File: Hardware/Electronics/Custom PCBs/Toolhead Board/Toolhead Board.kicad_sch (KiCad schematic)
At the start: 6 parts, among them U1 SE8650X2-HF, U2 XC6206P332MR

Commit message: Make some updates
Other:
- added sheet Load Cell Amplifiers (amps.kicad_sch)
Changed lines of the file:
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@@
     )
   )
-  (sheet (at 115.57 58.42) (size 12.7 3.81) (fields_autoplaced)
+  (sheet (at 95.25 19.05) (size 12.7 3.81) (fields_autoplaced)
     (stroke (width 0.1524) (type solid))
     (fill (color 0 0 0 0.0000))
-    (property "Sheetname" "Stepper Driver" (at 115.57 57.7084 0)
+    (property "Sheetname" "Stepper Driver" (at 95.25 18.3384 0)
       (effects (font (size 1.27 1.27)) (justify left bottom))
     )
-    (property "Sheetfile" "stepper.kicad_sch" (at 115.57 62.8146 0)
+    (property "Sheetfile" "stepper.kicad_sch" (at 95.25 23.4446 0)
       (effects (font (size 1.27 1.27)) (justify left top))
     )
@@
       )
     )
+  )
+  (sheet (at 100.33 35.56) (size 12.7 3.81) (fields_autoplaced)
+    (stroke (width 0.1524) (type solid))
+    (fill (color 0 0 0 0.0000))
+    (property "Sheetname" "Load Cell Amplifiers" (at 100.33 34.8484 0)
+      (effects (font (size 1.27 1.27)) (justify left bottom))
+    )
+    (property "Sheetfile" "amps.kicad_sch" (at 100.33 39.9546 0)
+      (effects (font (size 1.27 1.27)) (justify left top))
+    )
+    (instances
+      (project "Toolhead Board"
+        (path "/a1747683-152e-4245-ab61-2d33ce6021ef" (page "5"))
+      )
+    )

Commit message: some updates
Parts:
- C1: renamed from C10; footprint Capacitor_SMD:C_0805_2012Metric -> (none); Digikey (none) -> 4713-GMC21X7R105K50NTCT-ND
- C2: renamed from C11; footprint Capacitor_SMD:C_0402_1005Metric -> (none)
- C3: renamed from C12; footprint Capacitor_SMD:C_0402_1005Metric -> (none)
- C4: renamed from C13; footprint Capacitor_SMD:C_0402_1005Metric -> (none)
- U1: value SE8650X2-HF -> LF15_TO220; footprint Package_TO_SOT_SMD:SOT-23 -> Package_TO_SOT_THT:TO-220-3_Vertical
- U2: value XC6206P332MR -> LF15_TO220; footprint Package_TO_SOT_SMD:SOT-23 -> Package_TO_SOT_THT:TO-220-3_Vertical
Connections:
- net +24V: now also U1.1 (VI); no longer U1.3 (VI)
- net +3.3V: now also U2.3 (VO); no longer U2.2 (VO)
- net +5V: now also U1.3 (VO), U2.1 (VI); no longer U1.2 (VO), U2.3 (VI)
- net GND: now also U1.2 (GND), U2.2 (GND); no longer U1.1 (GND), U2.1 (GND)
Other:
- moved on the sheet: C1, C2, C3, C4, U1, U2

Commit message: Work on toolhead board more
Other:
- added sheet Accelerometer (accel.kicad_sch)
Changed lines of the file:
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@@
+    )
+  )
+  (sheet (at 48.26 31.75) (size 12.7 3.81) (fields_autoplaced)
+    (stroke (width 0.1524) (type solid))
+    (fill (color 0 0 0 0.0000))
+    (property "Sheetname" "Accelerometer" (at 48.26 31.0384 0)
+      (effects (font (size 1.27 1.27)) (justify left bottom))
+    )
+    (property "Sheetfile" "accel.kicad_sch" (at 48.26 36.1446 0)
+      (effects (font (size 1.27 1.27)) (justify left top))
+    )
+    (instances
+      (project "Toolhead Board"
+        (path "/a1747683-152e-4245-ab61-2d33ce6021ef" (page "6"))
+      )
     )
   )
@@
     )
   )
-  (sheet (at 100.33 35.56) (size 12.7 3.81) (fields_autoplaced)
+  (sheet (at 20.32 31.75) (size 12.7 3.81) (fields_autoplaced)
     (stroke (width 0.1524) (type solid))
     (fill (color 0 0 0 0.0000))
-    (property "Sheetname" "Load Cell Amplifiers" (at 100.33 34.8484 0)
+    (property "Sheetname" "Load Cell Amplifiers" (at 20.32 31.0384 0)
       (effects (font (size 1.27 1.27)) (justify left bottom))
     )
-    (property "Sheetfile" "amps.kicad_sch" (at 100.33 39.9546 0)
+    (property "Sheetfile" "amps.kicad_sch" (at 20.32 36.1446 0)
       (effects (font (size 1.27 1.27)) (justify left top))
     )

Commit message: Remove locks
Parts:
- added TP1, TP2: TestPoint, symbol Connector:TestPoint
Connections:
- new net SCL: TP2.1
- new net SDA: TP1.1
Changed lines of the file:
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@@
     (stroke (width 0) (type default))
+  )
+  (global_label "SCL" (shape input) (at 168.91 71.12 180) (fields_autoplaced)
+    (effects (font (size 1.27 1.27)) (justify right))
+    (property "Intersheetrefs" "${INTERSHEET_REFS}" (at 162.4172 71.12 0)
+      (effects (font (size 1.27 1.27)) (justify right) hide)
+    )
+  )
+  (global_label "SDA" (shape input) (at 168.91 63.5 180) (fields_autoplaced)
+    (effects (font (size 1.27 1.27)) (justify right))
+    (property "Intersheetrefs" "${INTERSHEET_REFS}" (at 162.3567 63.5 0)
+      (effects (font (size 1.27 1.27)) (justify right) hide)
+    )
   )
   (symbol (lib_id "power:PWR_FLAG") (at 179.07 31.75 180) (unit 1)
@@
         (path "/f7dd46fe-2ecb-430c-955f-2b30ea53e447"
           (reference "C10") (unit 1)
+        )
+      )
+    )
+  )
+  (symbol (lib_id "Connector:TestPoint") (at 168.91 71.12 270) (unit 1)
+    (in_bom yes) (on_board yes) (dnp no) (fields_autoplaced)
+    (property "Reference" "TP2" (at 173.99 69.85 90)
+      (effects (font (size 1.27 1.27)) (justify left))
+    )
+    (property "Value" "TestPoint" (at 173.99 72.39 90)
+      (effects (font (size 1.27 1.27)) (justify left))
+    )
+    (property "Footprint" "" (at 168.91 76.2 0)
+      (effects (font (size 1.27 1.27)) hide)
+    )
+    (property "Datasheet" "~" (at 168.91 76.2 0)
+      (effects (font (size 1.27 1.27)) hide)
+    )
+    (pin "1")
+    (instances
+      (project "Toolhead Board"
+        (path "/a1747683-152e-4245-ab61-2d33ce6021ef"
+          (reference "TP2") (unit 1)
         )
       )
@@
         )
       )
+    )
+  )
+  (symbol (lib_id "Connector:TestPoint") (at 168.91 63.5 270) (unit 1)
+    (in_bom yes) (on_board yes) (dnp no) (fields_autoplaced)
+    (property "Reference" "TP1" (at 173.99 62.23 90)
+      (effects (font (size 1.27 1.27)) (justify left))
+    )
+    (property "Value" "TestPoint" (at 173.99 64.77 90)
+      (effects (font (size 1.27 1.27)) (justify left))
+    )
+    (property "Footprint" "" (at 168.91 68.58 0)
+      (effects (font (size 1.27 1.27)) hide)
+    )
+    (property "Datasheet" "~" (at 168.91 68.58 0)
+      (effects (font (size 1.27 1.27)) hide)
+    )
+    (pin "1")
+    (instances
+      (project "Toolhead Board"
+        (path "/a1747683-152e-4245-ab61-2d33ce6021ef"
+          (reference "TP1") (unit 1)
+        )
+      )

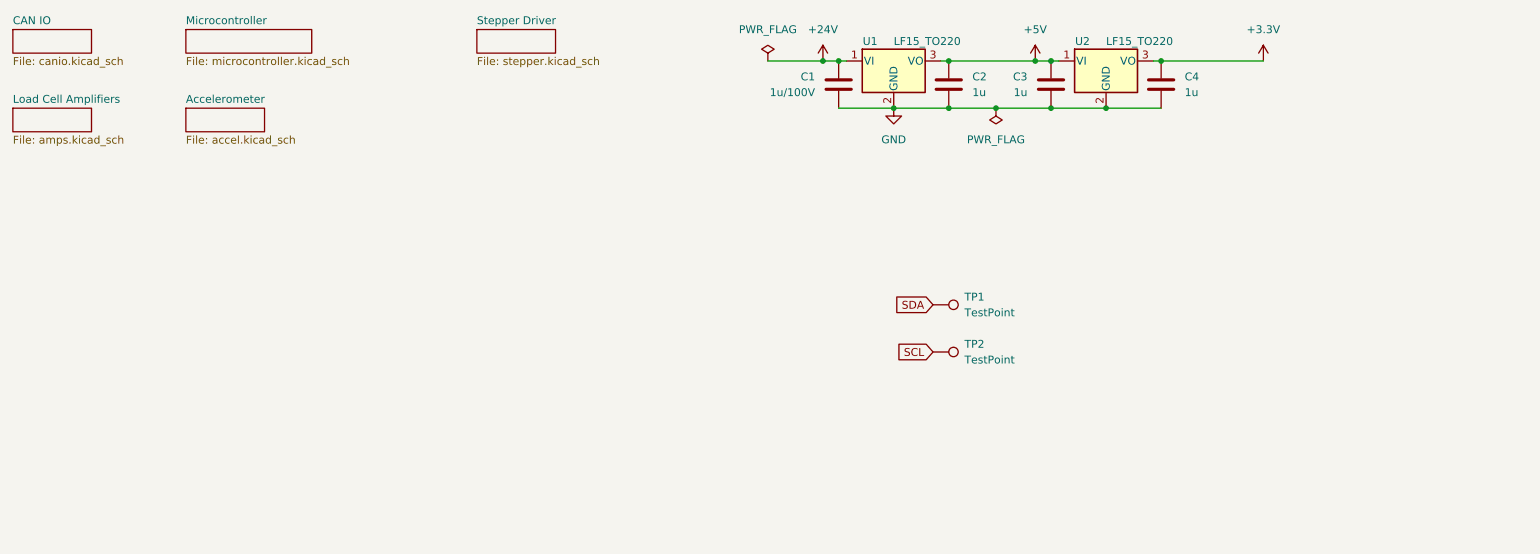
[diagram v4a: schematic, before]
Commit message: Finish Toolhead Schematic
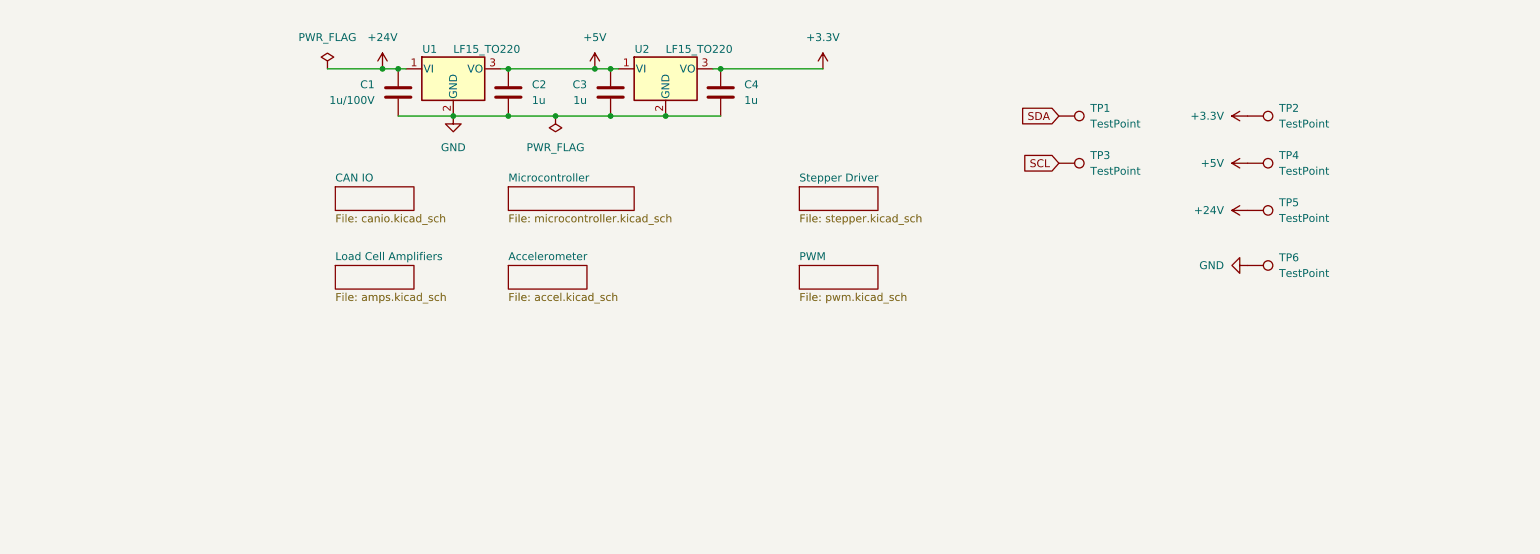
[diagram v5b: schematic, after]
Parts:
- added TP2, TP4, TP5, TP6: TestPoint, symbol Connector:TestPoint
- C2, C3, C4: Digikey (none) -> 1276-1102-1-ND
- U1: Digikey (none) -> 497-3436-5-ND
- U2: Digikey (none) -> 31-AZ1117CH2-3.3TRG1CT-ND
- renumbered TP2 to TP3
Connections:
- net +24V: now also TP5.1
- net +3.3V: now also TP2.1
- net +5V: now also TP4.1
- net GND: now also TP6.1
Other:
- added sheet PWM (pwm.kicad_sch)
- moved on the sheet: C1, C2, C3, C4, TP1, TP3, U1, U2

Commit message: Updated Footprints
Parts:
- C1: footprint (none) -> Capacitor_SMD:C_0805_2012Metric_Pad1.18x1.45mm_HandSolder
- C2, C3, C4: footprint (none) -> Capacitor_SMD:C_0603_1608Metric_Pad1.08x0.95mm_HandSolder
- TP1, TP2, TP3, TP4, TP5: footprint (none) -> TestPoint:TestPoint_Pad_D1.5mm
- TP6: footprint (none) -> TestPoint:TestPoint_Pad_1.5x1.5mm

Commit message: Get basic Toolhead Board outline
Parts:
- added H1, H2, H3, H4, H5, H6, H7, H8, H9: MountingHole, MountingHole:MountingHole_3.2mm_M3_DIN965_Pad, symbol Mechanical:MountingHole

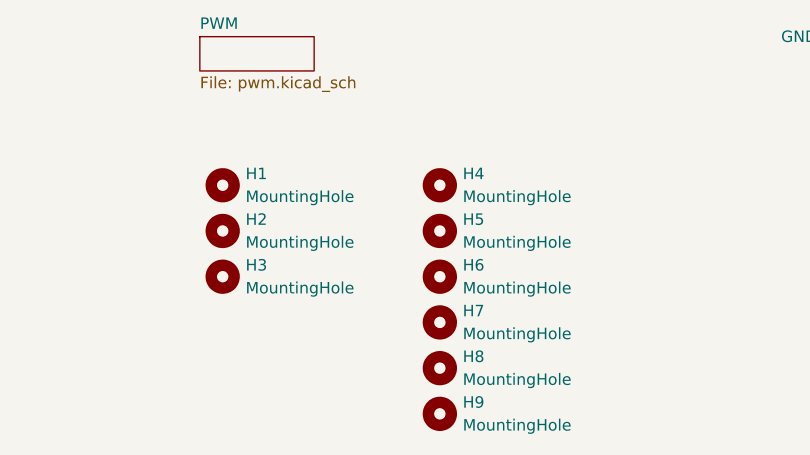
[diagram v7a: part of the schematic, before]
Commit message: Begin layout and routing of toolhead board
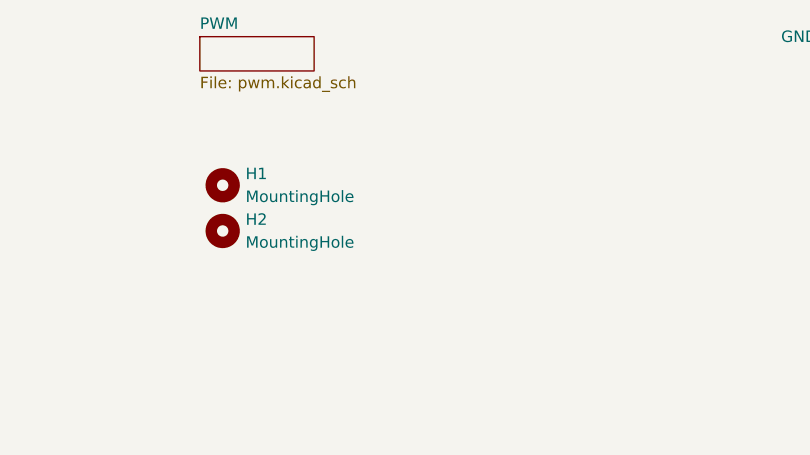
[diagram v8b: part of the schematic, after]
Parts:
- removed H3, H4, H5, H6, H7, H8, H9: MountingHole, MountingHole:MountingHole_3.2mm_M3_DIN965_Pad, symbol Mechanical:MountingHole
